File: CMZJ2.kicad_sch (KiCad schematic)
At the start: 114 parts, among them CON1 I2S, CON2 Display, CON3 OUT, CON4 IN, Q1 BC850, Q2 BC850

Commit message: HW Rev 1.08
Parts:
- renumbered C2 to C1, C7 to C10, C9 to C11, C8 to C12, C10 to C13, C4 to C14, C11 to C15, C3 to C16, C6 to C17, C18 to C2, C19 to C3, C20 to C4, C21 to C6, C22 to C7, C1 to C8, C16 to C9, CON2 to CON1, CON3 to CON2, CON4 to CON3, CON1 to CON4, D5 to D1, D1 to D5, DB91 to DB1, DB92 to DB2, DB93 to DB3, JP5 to JP2, JP2 to JP5, L4 to L2, L5 to L3, Q2 to Q1, Q1 to Q2, R49 to R1, R31 to R10, R56 to R11, R57 to R15, R15 to R16, R18 to R17, R19 to R18, R20 to R19, R7 to R2, R23 to R20, R55 to R21, R37 to R22, R47 to R23, R54 to R24, R51 to R25, R1 to R26, R2 to R27, R3 to R28, R4 to R29, R26 to R3, R34 to R30, R40 to R31, R42 to R32, R44 to R33, R53 to R34, R52 to R35, R6 to R36, R8 to R37, R11 to R38, R16 to R39, R33 to R4, R21 to R40, R27 to R41, R32 to R42, R38 to R43, R43 to R44, R48 to R45, R50 to R46, R9 to R47, R10 to R48, R24 to R49, R22 to R5, R30 to R50, R35 to R51, R41 to R52, R45 to R53, R17 to R54, R5 to R55, R39 to R56, R46 to R57, R28 to R6, R29 to R7, R36 to R8, R25 to R9
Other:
- moved on the sheet: C8, CON4, PWR1, PWR2, R26, R27, R28, R29, SC1, SD1, UART1

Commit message: HW Rev 1.09
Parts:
- removed C7: 1u, LIBS:Medved_CP_Radial_D5.0mm_P2.50mm, symbol Device:C_Polarized_Small
- removed L2, L3: LED, LED_SMD:LED_0805_2012Metric_Pad1.15x1.40mm_HandSolder, symbol Device:LED
- removed R11, R15: 1K, Resistor_SMD:R_0805_2012Metric_Pad1.20x1.40mm_HandSolder, symbol Device:R
- renumbered C2 to C1, C11 to C10, C12 to C11, C13 to C12, C14 to C13, C15 to C14, C16 to C15, C17 to C16, C3 to C2, C4 to C3, C1 to C4, C8 to C7, C9 to C8, C10 to C9, CON4 to JP7, JP7 to JP8, R2 to R1, R12 to R10, R13 to R11, R14 to R12, R16 to R13, R17 to R14, R18 to R15, R1 to R16, R19 to R17, R20 to R18, R21 to R19, R3 to R2, R22 to R20, R23 to R21, R24 to R22, R25 to R23, R26 to R24, R27 to R25, R28 to R26, R29 to R27, R30 to R28, R31 to R29, R4 to R3, R32 to R30, R33 to R31, R34 to R32, R35 to R33, R36 to R34, R37 to R35, R38 to R36, R39 to R37, R40 to R38, R41 to R39, R5 to R4, R42 to R40, R43 to R41, R44 to R42, R45 to R43, R46 to R44, R47 to R45, R48 to R46, R49 to R47, R50 to R48, R51 to R49, R6 to R5, R52 to R50, R53 to R51, R54 to R52, R55 to R53, R56 to R54, R57 to R55, R7 to R6, R8 to R7, R9 to R8, R10 to R9
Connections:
- net CTS_IN: now also DB1.8; no longer DB1.7
- net CTS_OUT: no longer MAX1.10 (T2IN)
- net RTS_IN: now also DB1.7; no longer DB1.8
- net RTS_OUT: no longer MAX1.9 (R2OUT)
- net RX_IN: now also DB1.2; no longer DB1.3
- net RX_OUT: no longer MAX1.12 (R1OUT)
- net TX_IN: now also DB1.3; no longer DB1.2
- net TX_OUT: no longer MAX1.11 (T1IN)
- new net CTS_MAX: MAX1.10 (T2IN)
- new net RTS_MAX: MAX1.9 (R2OUT)
- new net RX_MAX: MAX1.12 (R1OUT)
- new net TX_MAX: MAX1.11 (T1IN)
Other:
- added sheet Shifter_CTS (level_shifter.kicad_sch)
- added sheet Shifter_RTS (level_shifter.kicad_sch)
- added sheet Shifter_RX (level_shifter.kicad_sch)
- added sheet Shifter_TX (level_shifter.kicad_sch)
- moved on the sheet: C1, C2, C3, C6, JP6, L1, MAX1, R16

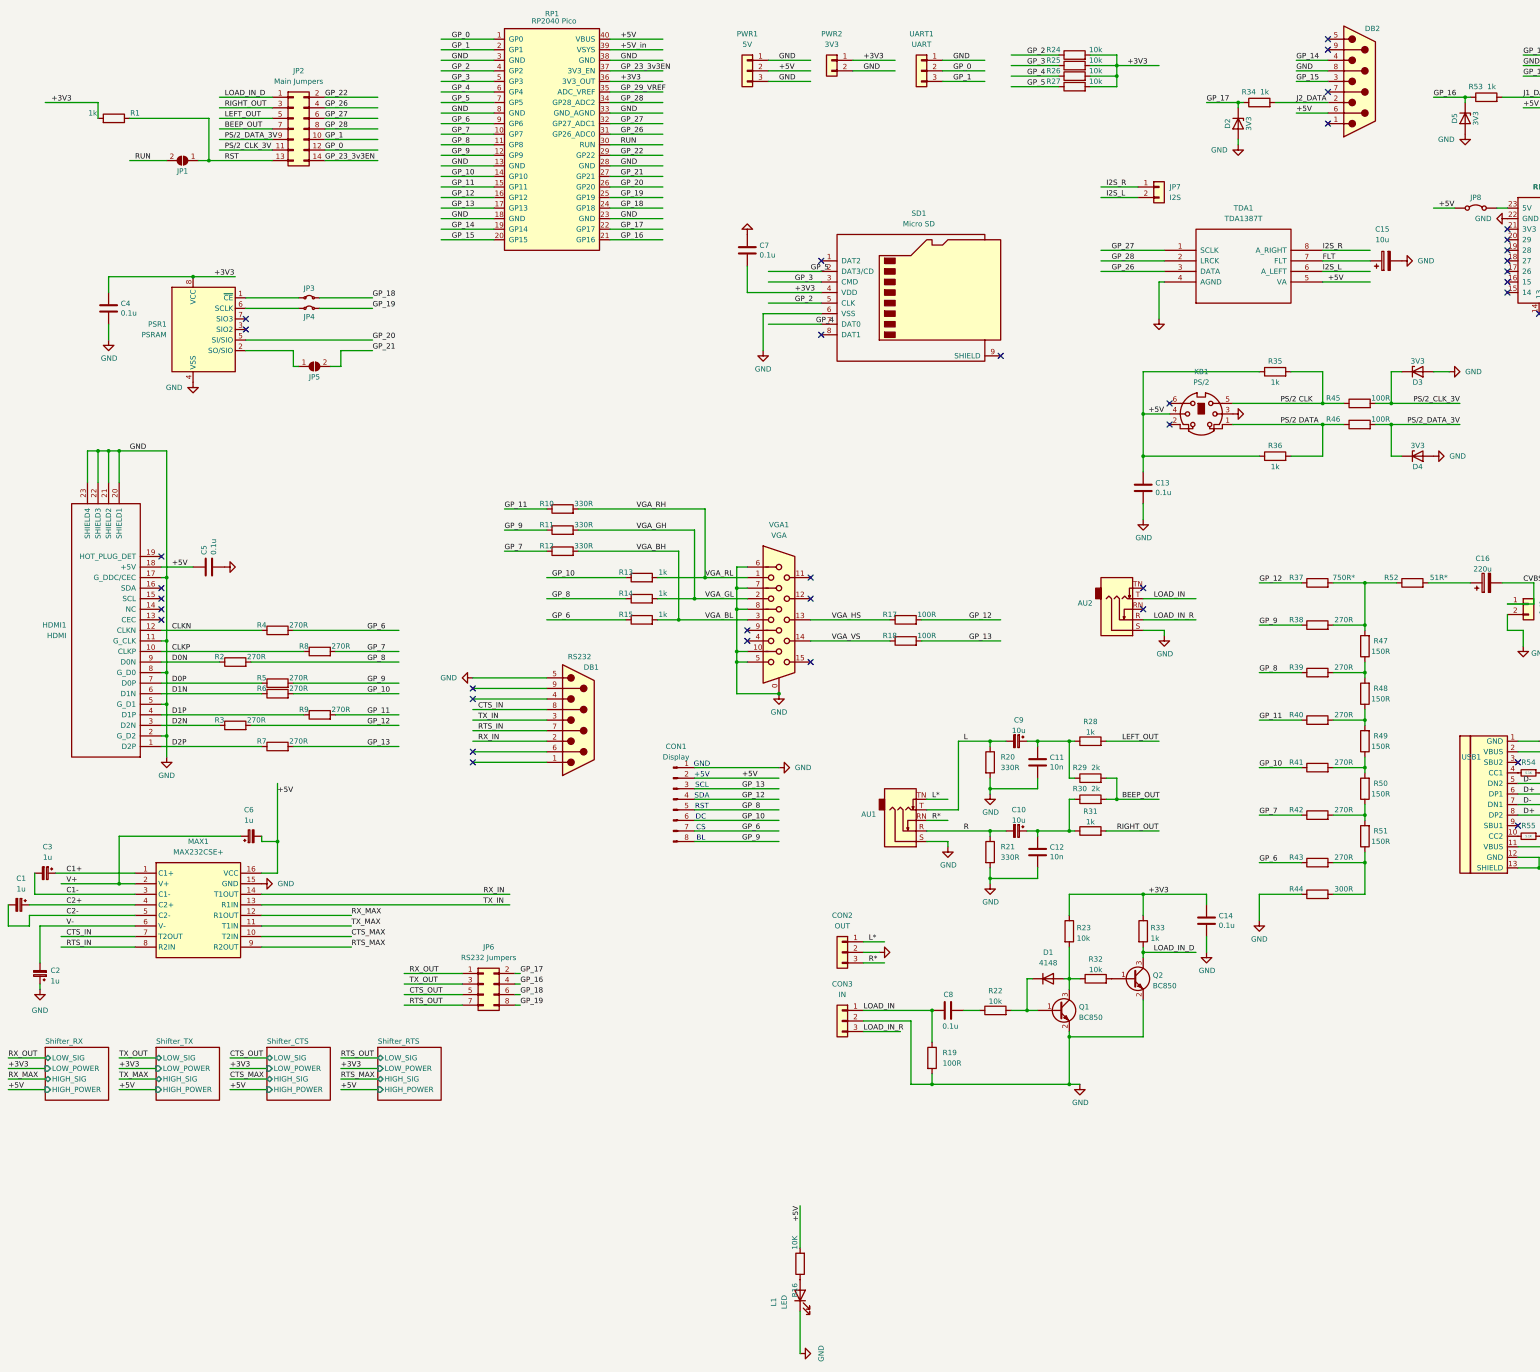
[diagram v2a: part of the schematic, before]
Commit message: MAX232-related changes
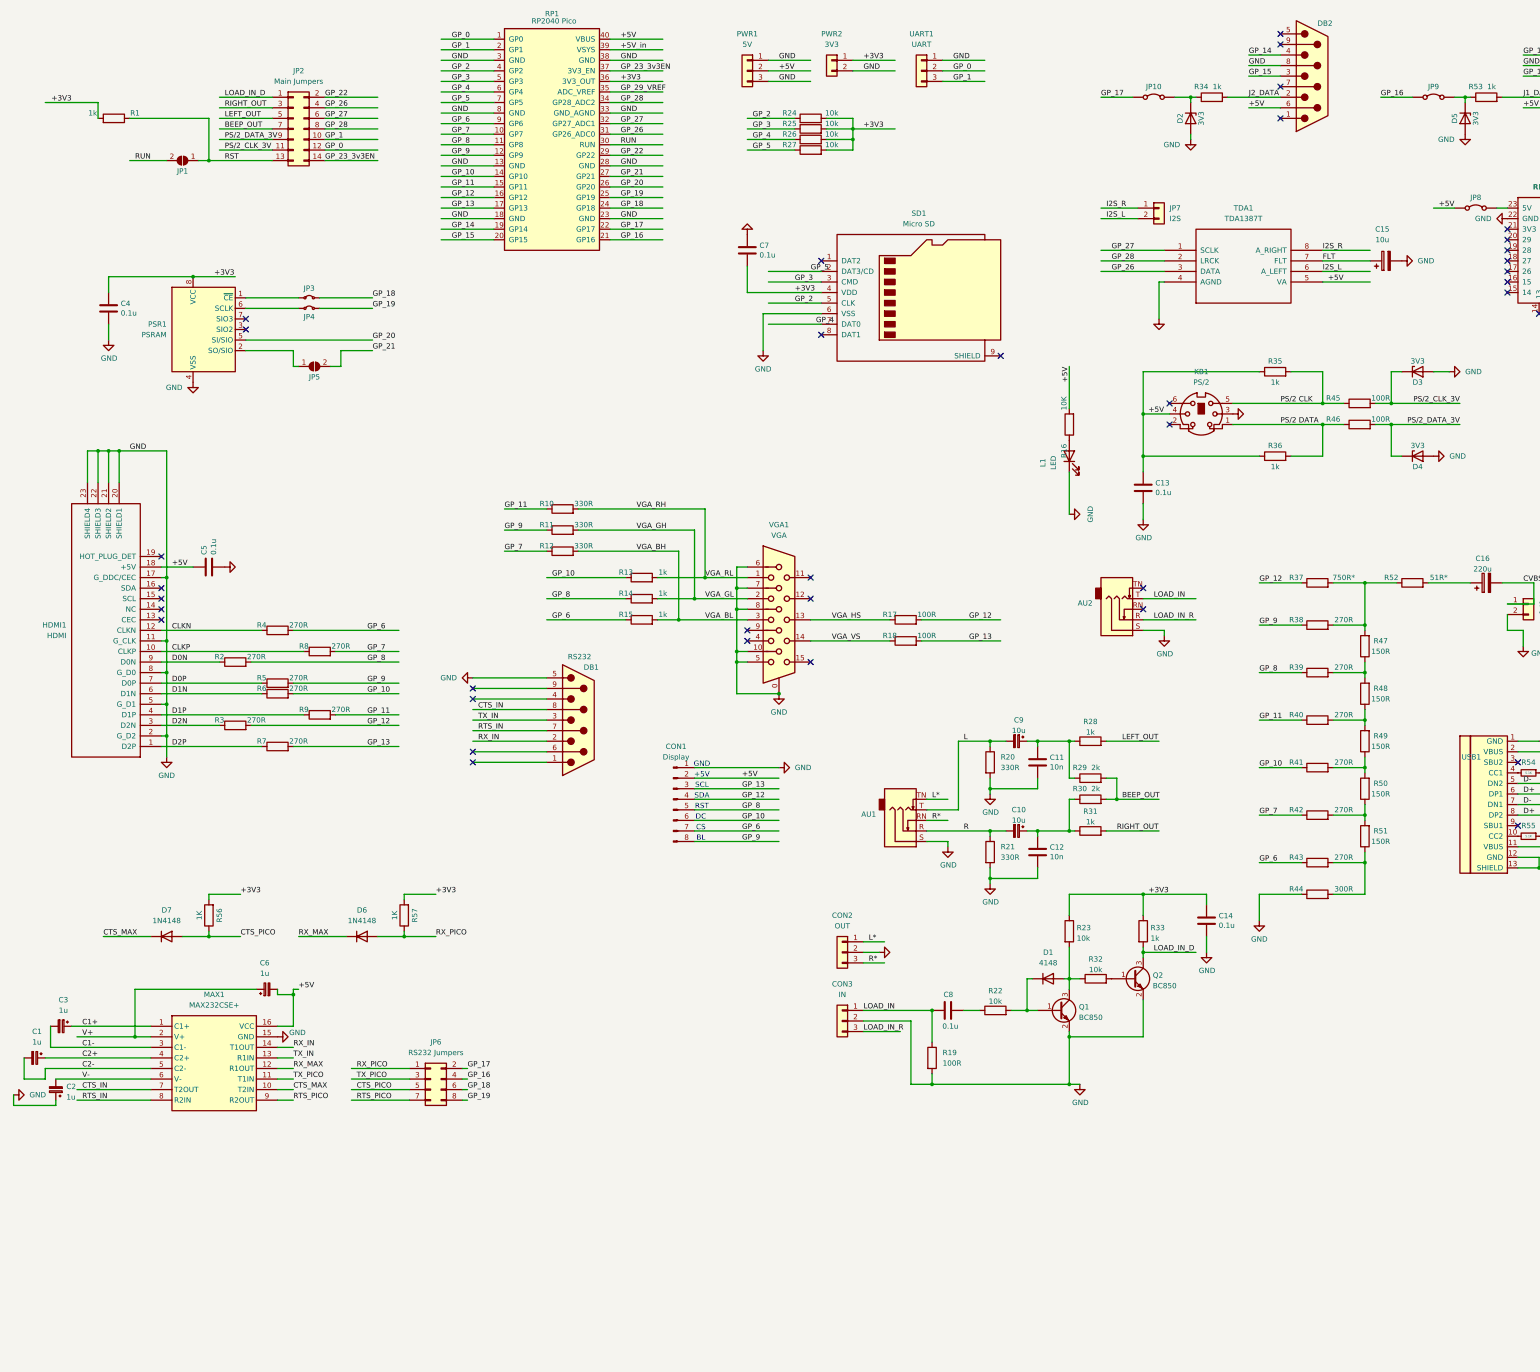
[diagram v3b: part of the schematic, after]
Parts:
- added D6, D7: 1N4148, LIBS:R_0805_PLUS, symbol Diode:1N4148
- added JP10, JP9: RP ZERO +5V Jumper, LIBS:Medved_PinHeader_1x02_P2.54mm_Vertical_R, symbol Jumper:Jumper_2_Bridged
- added R56, R57: 1K, Resistor_SMD:R_0805_2012Metric_Pad1.20x1.40mm_HandSolder, symbol Device:R
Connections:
- net RTS_OUT is gone; now on net RTS_PICO: JP6.7 (Pin_7)
- net TX_OUT is gone; now on net TX_PICO: JP6.3 (Pin_3)
- net +3V3: now also R56.2, R57.2
- net CTS_MAX: now also D7.1 (K)
- net GP_16: now also JP9.1 (A); no longer D5.1 (K), R53.1
- net GP_17: now also JP10.1 (A); no longer D2.1 (K), R34.1
- net RX_MAX: now also D6.1 (K)
- net CTS_OUT renamed CTS_PICO
- net CTS_PICO: now also D7.2 (A), R56.1
- net RTS_MAX renamed RTS_PICO
- net RX_OUT renamed RX_PICO
- net RX_PICO: now also D6.2 (A), R57.1
- net TX_MAX renamed TX_PICO
- new net: D2.1 (K), JP10.2 (B), R34.1
- new net: D5.1 (K), JP9.2 (B), R53.1
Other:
- removed sheet Shifter_CTS
- removed sheet Shifter_RTS
- removed sheet Shifter_RX
- removed sheet Shifter_TX
- moved on the sheet: C1, C2, C3, C6, D2, DB2, JP6, JP7, L1, MAX1, R16, R24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

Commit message: HW Rev 1.10
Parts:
- added SW1: SW_Push_Dual, LIBS:Button_SMD_3x3x2, symbol Switch:SW_Push_Dual
- DB1, DB2, DB3: footprint Connector_Dsub:DSUB-9_Male_EdgeMount_P2.77mm -> LIBS:DSUB-9_Joystick
- renumbered D7 to D1, D6 to D2, D1 to D3, D2 to D4, D3 to D5, D4 to D6, D5 to D7, JP8 to JP10, JP10 to JP7, JP7 to JP8, R9 to R10, R57 to R11, R10 to R12, R11 to R13, R12 to R14, R13 to R15, R14 to R16, R15 to R17, R24 to R18, R25 to R19, R56 to R2, R26 to R20, R27 to R21, R17 to R22, R18 to R23, R19 to R24, R20 to R25, R21 to R26, R22 to R27, R16 to R28, R23 to R29, R2 to R3, R28 to R30, R29 to R31, R30 to R32, R31 to R33, R32 to R34, R33 to R35, R34 to R36, R35 to R37, R36 to R38, R37 to R39, R3 to R4, R38 to R40, R39 to R41, R40 to R42, R41 to R43, R42 to R44, R43 to R45, R44 to R46, R45 to R47, R46 to R48, R47 to R49, R4 to R5, R48 to R50, R49 to R51, R50 to R52, R51 to R53, R52 to R54, R53 to R55, R54 to R56, R55 to R57, R5 to R6, R6 to R7, R7 to R8, R8 to R9
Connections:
- net CTS_MAX: now also MAX1.9 (R2OUT); no longer MAX1.10 (T2IN)
- net GND: now also SW1.3, SW1.4
- net RTS_PICO: now also MAX1.10 (T2IN); no longer MAX1.9 (R2OUT)
- net RUN: now also SW1.1, SW1.2
- net at DB1.1: now also DB1.4, DB1.6
- no-connect marks 52 -> 49
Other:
- company: (none) -> Mikhail Matveev
- title: (none) -> Frank
- moved on the sheet: C6, DB1

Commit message: HW Rev 1.12
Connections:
- net CTS_IN: now also DB1.7; no longer DB1.8
- net RTS_IN: now also DB1.8; no longer DB1.7
- net RX_IN: now also DB1.3; no longer DB1.2
- net TX_IN: now also DB1.2; no longer DB1.3
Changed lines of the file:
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@@
 	(title_block
 		(title "Frank")
-		(date "2024-10-05")
-		(rev "1.10")
+		(date "2024-10-23")
+		(rev "1.12")
 		(company "Mikhail Matveev")
 		(comment 1 "https://rh1.dev")
@@
 		)
 	)
-	(label "CTS_IN"
+	(label "RTS_IN"
 		(at 137.16 252.73 0)
 		(fields_autoplaced yes)
@@
 		)
 	)
-	(label "TX_IN"
+	(label "RX_IN"
 		(at 137.16 255.27 0)
 		(fields_autoplaced yes)
@@
 		)
 	)
-	(label "RX_IN"
+	(label "TX_IN"
 		(at 137.16 260.35 0)
 		(fields_autoplaced yes)
@@
 		)
 	)
-	(label "RTS_IN"
+	(label "CTS_IN"
 		(at 137.16 257.81 0)
 		(fields_autoplaced yes)

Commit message: Minor updates
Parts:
- C13, C14, C4, C5, C7, C8: value 0.1u -> 100n
- R1, R35, R36, R37, R38, R55: value 1k -> 1K
- R18, R19, R20, R21, R27, R29, R34: value 10k -> 10K
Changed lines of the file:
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@@
 			)
 		)
-		(property "Value" "1k"
+		(property "Value" "1K"
 			(at 304.8 35.56 90)
 			(effects
@@
 			)
 		)
-		(property "Value" "10k"
+		(property "Value" "10K"
 			(at 275.59 248.0111 90)
 			(effects
@@
 			)
 		)
-		(property "Value" "10k"
+		(property "Value" "10K"
 			(at 271.018 240.4622 0)
 			(effects
@@
 			)
 		)
-		(property "Value" "10k"
+		(property "Value" "10K"
 			(at 212.09 41.91 90)
 			(effects
@@
 			)
 		)
-		(property "Value" "0.1u"
+		(property "Value" "100n"
 			(at 305.181 237.363 0)
 			(effects
@@
 			)
 		)
-		(property "Value" "0.1u"
+		(property "Value" "100n"
 			(at 194.691 76.073 0)
 			(effects
@@
 			)
 		)
-		(property "Value" "0.1u"
+		(property "Value" "100n"
 			(at 242.57 261.62 90)
 			(effects
@@
 		(fields_autoplaced yes)
 		(property "Reference" "R27"
-			(at 251.46 253.0942 90)
+			(at 251.46 251.46 90)
 			(effects
 				(font
@@
 			)
 		)
-		(property "Value" "10k"
-			(at 251.46 255.6311 90)
+		(property "Value" "10K"
+			(at 251.46 254 90)
 			(effects
 				(font
@@
 			)
 		)
-		(property "Value" "0.1u"
+		(property "Value" "100n"
 			(at 41.021 90.043 0)
 			(effects
@@
 			)
 		)
-		(property "Value" "1k"
+		(property "Value" "1K"
 			(at 318.77 127 90)
 			(effects
@@
 			)
 		)
-		(property "Value" "10k"
+		(property "Value" "10K"
 			(at 212.09 46.99 90)
 			(effects
@@
 			)
 		)
-		(property "Value" "1k"
+		(property "Value" "1K"
 			(at 288.798 240.4622 0)
 			(effects
@@
 			)
 		)
-		(property "Value" "0.1u"
+		(property "Value" "100n"
 			(at 63.373 148.209 0)
 			(effects
@@
 			)
 		)
-		(property "Value" "10k"
+		(property "Value" "10K"
 			(at 212.09 44.45 90)
 			(effects
@@
 			)
 		)
-		(property "Value" "10k"
+		(property "Value" "10K"
 			(at 212.09 49.53 90)
 			(effects
@@
 			)
 		)
-		(property "Value" "0.1u"
+		(property "Value" "100n"
 			(at 289.941 133.223 0)
 			(effects
@@
 			)
 		)
-		(property "Value" "1k"
+		(property "Value" "1K"
 			(at 370.84 35.56 90)
 			(effects
@@
 			)
 		)
-		(property "Value" "1k"
+		(property "Value" "1K"
 			(at 34.29 41.91 90)
 			(effects
@@
 			)
 		)
-		(property "Value" "1k"
+		(property "Value" "1K"
 			(at 318.77 106.68 90)
 			(effects
